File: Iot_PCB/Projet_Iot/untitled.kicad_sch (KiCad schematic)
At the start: 2 parts, among them J21 Conn_01x15_Pin, J22 Conn_01x15_Pin

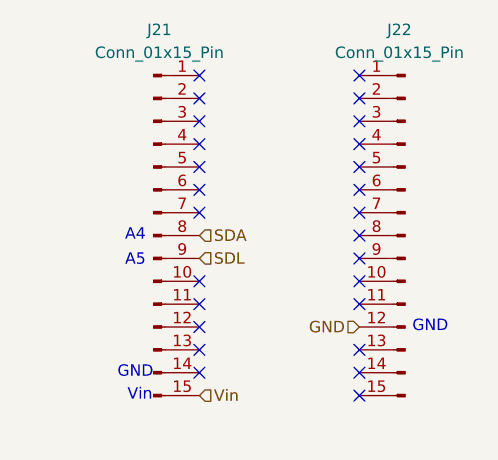
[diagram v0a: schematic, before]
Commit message: remplacement des grove lora par des vrais
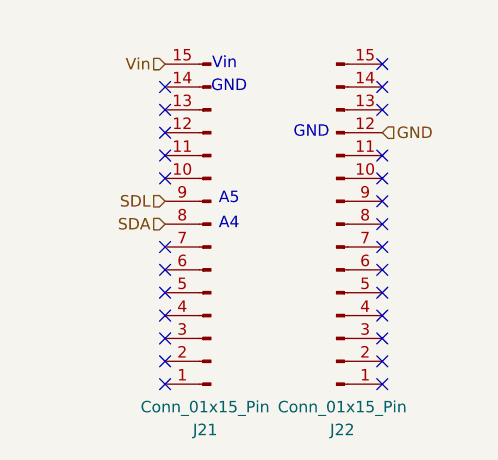
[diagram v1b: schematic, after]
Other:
- moved on the sheet: J21, J22
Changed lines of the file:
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@@
 	(paper "A4")
 	(no_connect
-		(at 133.35 90.17)
-	)
-	(no_connect
-		(at 115.57 77.47)
-	)
-	(no_connect
-		(at 133.35 77.47)
-	)
-	(no_connect
-		(at 133.35 110.49)
-	)
-	(no_connect
-		(at 133.35 105.41)
-	)
-	(no_connect
-		(at 133.35 87.63)
-	)
-	(no_connect
-		(at 133.35 92.71)
-	)
-	(no_connect
-		(at 115.57 74.93)
-	)
-	(no_connect
-		(at 133.35 80.01)
-	)
-	(no_connect
-		(at 115.57 87.63)
-	)
-	(no_connect
-		(at 115.57 82.55)
-	)
-	(no_connect
-		(at 133.35 97.79)
-	)
-	(no_connect
-		(at 115.57 107.95)
-	)
-	(no_connect
-		(at 133.35 82.55)
-	)
-	(no_connect
-		(at 133.35 95.25)
-	)
-	(no_connect
-		(at 115.57 90.17)
-	)
-	(no_connect
-		(at 115.57 97.79)
-	)
-	(no_connect
-		(at 115.57 85.09)
-	)
-	(no_connect
-		(at 133.35 107.95)
-	)
-	(no_connect
-		(at 115.57 105.41)
-	)
-	(no_connect
-		(at 115.57 80.01)
-	)
-	(no_connect
-		(at 115.57 102.87)
-	)
-	(no_connect
-		(at 133.35 74.93)
-	)
-	(no_connect
-		(at 133.35 100.33)
-	)
-	(no_connect
-		(at 133.35 85.09)
-	)
-	(no_connect
-		(at 115.57 100.33)
+		(at 135.89 93.98)
+	)
+	(no_connect
+		(at 111.76 106.68)
+	)
+	(no_connect
+		(at 135.89 106.68)
+	)
+	(no_connect
+		(at 135.89 73.66)
+	)
+	(no_connect
+		(at 135.89 78.74)
+	)
+	(no_connect
+		(at 135.89 96.52)
+	)
+	(no_connect
+		(at 135.89 91.44)
+	)
+	(no_connect
+		(at 111.76 109.22)
+	)
+	(no_connect
+		(at 135.89 104.14)
+	)
+	(no_connect
+		(at 111.76 96.52)
+	)
+	(no_connect
+		(at 111.76 101.6)
+	)
+	(no_connect
+		(at 135.89 86.36)
+	)
+	(no_connect
+		(at 111.76 76.2)
+	)
+	(no_connect
+		(at 135.89 101.6)
+	)
+	(no_connect
+		(at 135.89 88.9)
+	)
+	(no_connect
+		(at 111.76 93.98)
+	)
+	(no_connect
+		(at 111.76 86.36)
+	)
+	(no_connect
+		(at 111.76 99.06)
+	)
+	(no_connect
+		(at 135.89 76.2)
+	)
+	(no_connect
+		(at 111.76 78.74)
+	)
+	(no_connect
+		(at 111.76 104.14)
+	)
+	(no_connect
+		(at 111.76 81.28)
+	)
+	(no_connect
+		(at 135.89 109.22)
+	)
+	(no_connect
+		(at 135.89 83.82)
+	)
+	(no_connect
+		(at 135.89 99.06)
+	)
+	(no_connect
+		(at 111.76 83.82)
 	)
 	(text "GND\n"
 		(exclude_from_sim no)
-		(at 141.224 102.87 0)
+		(at 128.016 81.28 0)
 		(effects
 			(font
@@
 	(text "A4\n"
 		(exclude_from_sim no)
-		(at 108.458 92.71 0)
+		(at 118.872 91.44 0)
 		(effects
 			(font
@@
 	(text "A5\n"
 		(exclude_from_sim no)
-		(at 108.458 95.504 0)
+		(at 118.872 88.646 0)
 		(effects
 			(font
@@
 	(text "GND"
 		(exclude_from_sim no)
-		(at 108.458 107.95 0)
+		(at 118.872 76.2 0)
 		(effects
 			(font
@@
 	(text "Vin"
 		(exclude_from_sim no)
-		(at 108.966 110.49 0)
+		(at 118.364 73.66 0)
 		(effects
 			(font
@@
 	(hierarchical_label "SDL"
 		(shape input)
-		(at 115.57 95.25 0)
-		(fields_autoplaced yes)
-		(effects
-			(font
-				(size 1.27 1.27)
-			)
-			(justify left)
+		(at 111.76 88.9 180)
+		(fields_autoplaced yes)
+		(effects
+			(font
+				(size 1.27 1.27)
+			)
+			(justify right)
 		)
 	)
 	(hierarchical_label "SDA"
 		(shape input)
-		(at 115.57 92.71 0)
-		(fields_autoplaced yes)
-		(effects
-			(font
-				(size 1.27 1.27)
-			)
-			(justify left)
+		(at 111.76 91.44 180)
+		(fields_autoplaced yes)
+		(effects
+			(font
+				(size 1.27 1.27)
+			)
+			(justify right)
 		)
 	)
 	(hierarchical_label "Vin"
 		(shape input)
-		(at 115.57 110.49 0)
-		(fields_autoplaced yes)
-		(effects
-			(font
-				(size 1.27 1.27)
-			)
-			(justify left)
+		(at 111.76 73.66 180)
+		(fields_autoplaced yes)
+		(effects
+			(font
+				(size 1.27 1.27)
+			)
+			(justify right)
 		)
 	)
 	(hierarchical_label "GND"
 		(shape input)
-		(at 133.35 102.87 180)
-		(fields_autoplaced yes)
-		(effects
-			(font
-				(size 1.27 1.27)
-			)
-			(justify right)
+		(at 135.89 81.28 0)
+		(fields_autoplaced yes)
+		(effects
+			(font
+				(size 1.27 1.27)
+			)
+			(justify left)
 		)
 	)
 	(symbol
 		(lib_id "Connector:Conn_01x15_Pin")
-		(at 138.43 92.71 0)
-		(mirror y)
+		(at 130.81 91.44 0)
+		(mirror x)
 		(unit 1)
 		(exclude_from_sim no)
@@
 		(dnp no)
 		(property "Reference" "J22"
-			(at 137.795 69.85 0)
+			(at 131.445 114.3 0)
 			(effects
 				(font
@@
 		)
 		(property "Value" "Conn_01x15_Pin"
-			(at 137.795 72.39 0)
+			(at 131.445 111.76 0)
 			(effects
 				(font
@@
 		)
 		(property "Footprint" ""
-			(at 138.43 92.71 0)
+			(at 130.81 91.44 0)
 			(effects
 				(font
@@
 		)
 		(property "Datasheet" "~"
-			(at 138.43 92.71 0)
+			(at 130.81 91.44 0)
 			(effects
 				(font
@@
 		)
 		(property "Description" "Generic connector, single row, 01x15, script generated"
-			(at 138.43 92.71 0)
+			(at 130.81 91.44 0)
 			(effects
 				(font
@@
 	(symbol
 		(lib_id "Connector:Conn_01x15_Pin")
-		(at 110.49 92.71 0)
+		(at 116.84 91.44 180)
 		(unit 1)
 		(exclude_from_sim no)
@@
 		(fields_autoplaced yes)
 		(property "Reference" "J21"
-			(at 111.125 69.85 0)
+			(at 116.205 114.3 0)
 			(effects
 				(font
@@
 		)
 		(property "Value" "Conn_01x15_Pin"
-			(at 111.125 72.39 0)
+			(at 116.205 111.76 0)
 			(effects
 				(font
@@
 		)
 		(property "Footprint" ""
-			(at 110.49 92.71 0)
+			(at 116.84 91.44 0)
 			(effects
 				(font
@@
 		)
 		(property "Datasheet" "~"
-			(at 110.49 92.71 0)
+			(at 116.84 91.44 0)
 			(effects
 				(font
@@
 		)
 		(property "Description" "Generic connector, single row, 01x15, script generated"
-			(at 110.49 92.71 0)
-			(effects
-				(font
+			(at 116.84 91.44 0)
+			(effects
+				(font

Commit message: build(kicad): add a trace to every schematic
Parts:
- J21, J22: footprint (none) -> Connector_PinHeader_2.54mm:PinHeader_1x15_P2.54mm_Vertical
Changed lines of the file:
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@@
 (kicad_sch
-	(version 20231120)
+	(version 20250114)
 	(generator "eeschema")
-	(generator_version "8.0")
+	(generator_version "9.0")
 	(paper "A4")
+	(text "GND\n"
+		(exclude_from_sim no)
+		(at 128.016 81.28 0)
+		(effects
+			(font
+				(size 1.27 1.27)
+			)
+		)
+	)
+	(text "A4\n"
+		(exclude_from_sim no)
+		(at 118.872 91.44 0)
+		(effects
+			(font
+				(size 1.27 1.27)
+			)
+		)
+	)
+	(text "A5\n"
+		(exclude_from_sim no)
+		(at 118.872 88.646 0)
+		(effects
+			(font
+				(size 1.27 1.27)
+			)
+		)
+	)
+	(text "GND"
+		(exclude_from_sim no)
+		(at 118.872 76.2 0)
+		(effects
+			(font
+				(size 1.27 1.27)
+			)
+		)
+	)
+	(text "Vin"
+		(exclude_from_sim no)
+		(at 118.364 73.66 0)
+		(effects
+			(font
+				(size 1.27 1.27)
+			)
+		)
+	)
 	(no_connect
 		(at 135.89 93.98)
@@
 		(at 111.76 83.82)
 	)
-	(text "GND\n"
-		(exclude_from_sim no)
-		(at 128.016 81.28 0)
-		(effects
-			(font
-				(size 1.27 1.27)
-			)
-		)
-	)
-	(text "A4\n"
-		(exclude_from_sim no)
-		(at 118.872 91.44 0)
-		(effects
-			(font
-				(size 1.27 1.27)
-			)
-		)
-	)
-	(text "A5\n"
-		(exclude_from_sim no)
-		(at 118.872 88.646 0)
-		(effects
-			(font
-				(size 1.27 1.27)
-			)
-		)
-	)
-	(text "GND"
-		(exclude_from_sim no)
-		(at 118.872 76.2 0)
-		(effects
-			(font
-				(size 1.27 1.27)
-			)
-		)
-	)
-	(text "Vin"
-		(exclude_from_sim no)
-		(at 118.364 73.66 0)
-		(effects
-			(font
-				(size 1.27 1.27)
-			)
-		)
-	)
 	(hierarchical_label "SDL"
 		(shape input)
 		(at 111.76 88.9 180)
-		(fields_autoplaced yes)
 		(effects
 			(font
@@
 		(shape input)
 		(at 111.76 91.44 180)
-		(fields_autoplaced yes)
 		(effects
 			(font
@@
 		(shape input)
 		(at 111.76 73.66 180)
-		(fields_autoplaced yes)
 		(effects
 			(font
@@
 		(shape input)
 		(at 135.89 81.28 0)
-		(fields_autoplaced yes)
 		(effects
 			(font
@@
 			)
 		)
-		(property "Footprint" ""
+		(property "Footprint" "Connector_PinHeader_2.54mm:PinHeader_1x15_P2.54mm_Vertical"
 			(at 130.81 91.44 0)
 			(effects
@@
 			)
 		)
-		(property "Footprint" ""
+		(property "Footprint" "Connector_PinHeader_2.54mm:PinHeader_1x15_P2.54mm_Vertical"
 			(at 116.84 91.44 0)
 			(effects

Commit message: pcb and schematic up to date
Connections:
- net interrupt_ia: now reaches J21.7 (Pin_7)
- no-connect marks 26 -> 25
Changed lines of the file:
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@@
-	)
-	(no_connect
-		(at 111.76 93.98)
 	)
 	(no_connect
@@
 		(at 111.76 83.82)
 	)
+	(hierarchical_label "interrupt_ia"
+		(shape input)
+		(at 111.76 93.98 180)
+		(effects
+			(font
+				(size 1.27 1.27)
+			)
+			(justify right)
+		)
+	)
 	(hierarchical_label "SDL"
